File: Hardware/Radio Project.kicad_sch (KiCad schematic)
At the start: 4 parts, among them J1 RJ45_Abracon_ARJP11A-MASA-B-A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, U1 Si4464, U2 Si4464, U3 STM32F407VGT6

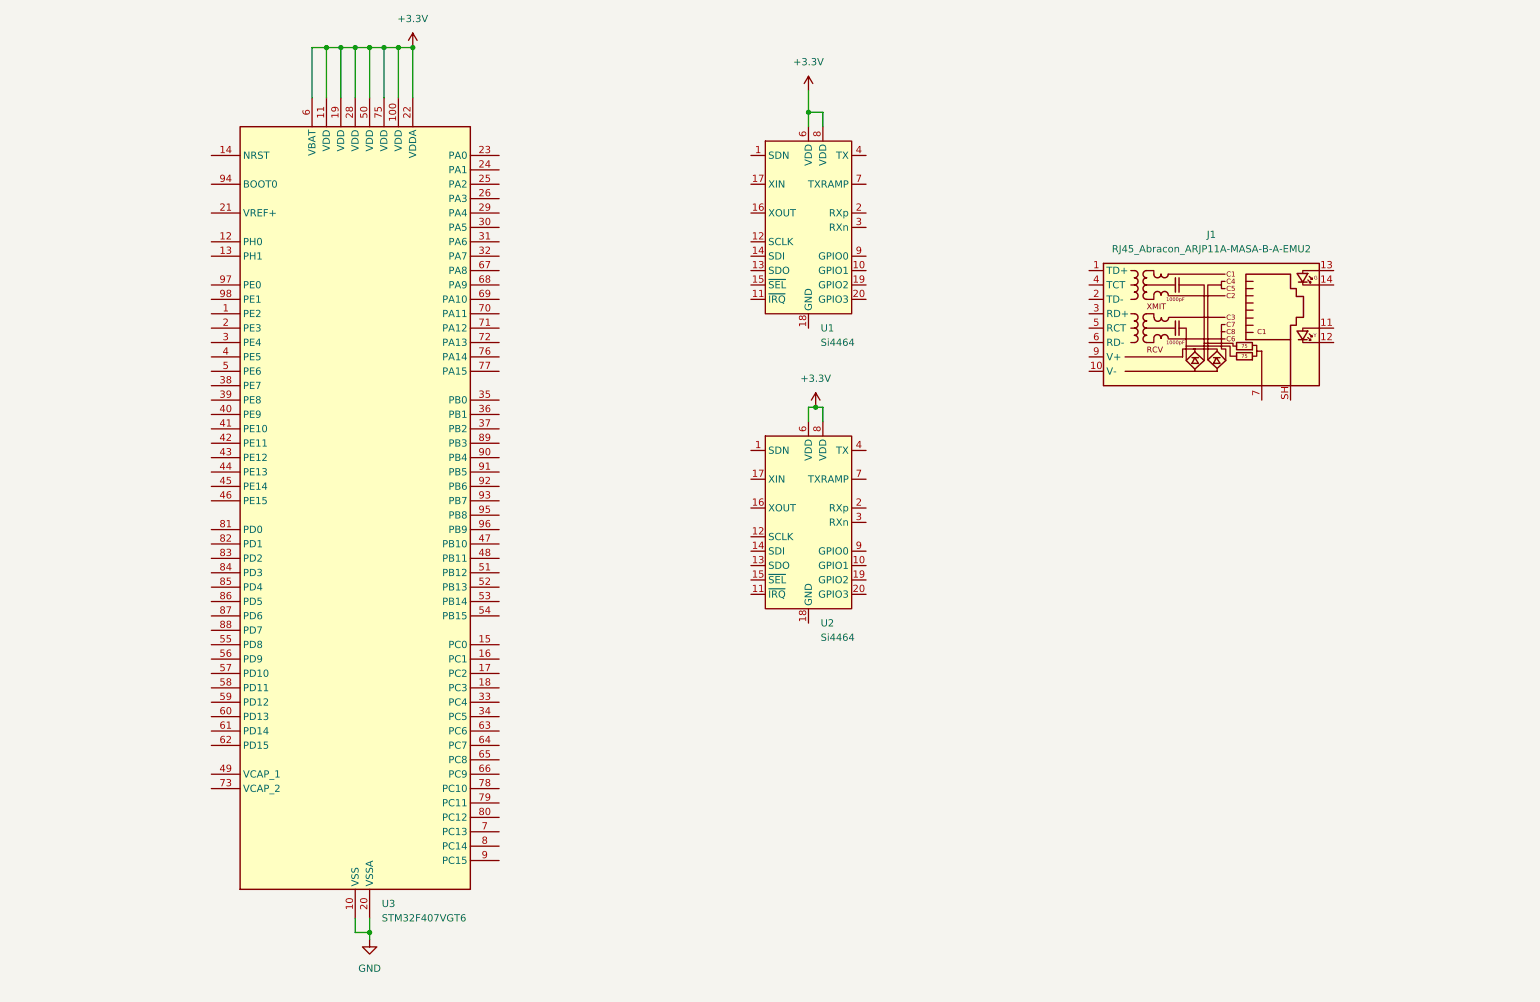
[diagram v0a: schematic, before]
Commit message: added SWD header and dip switches for boot modes
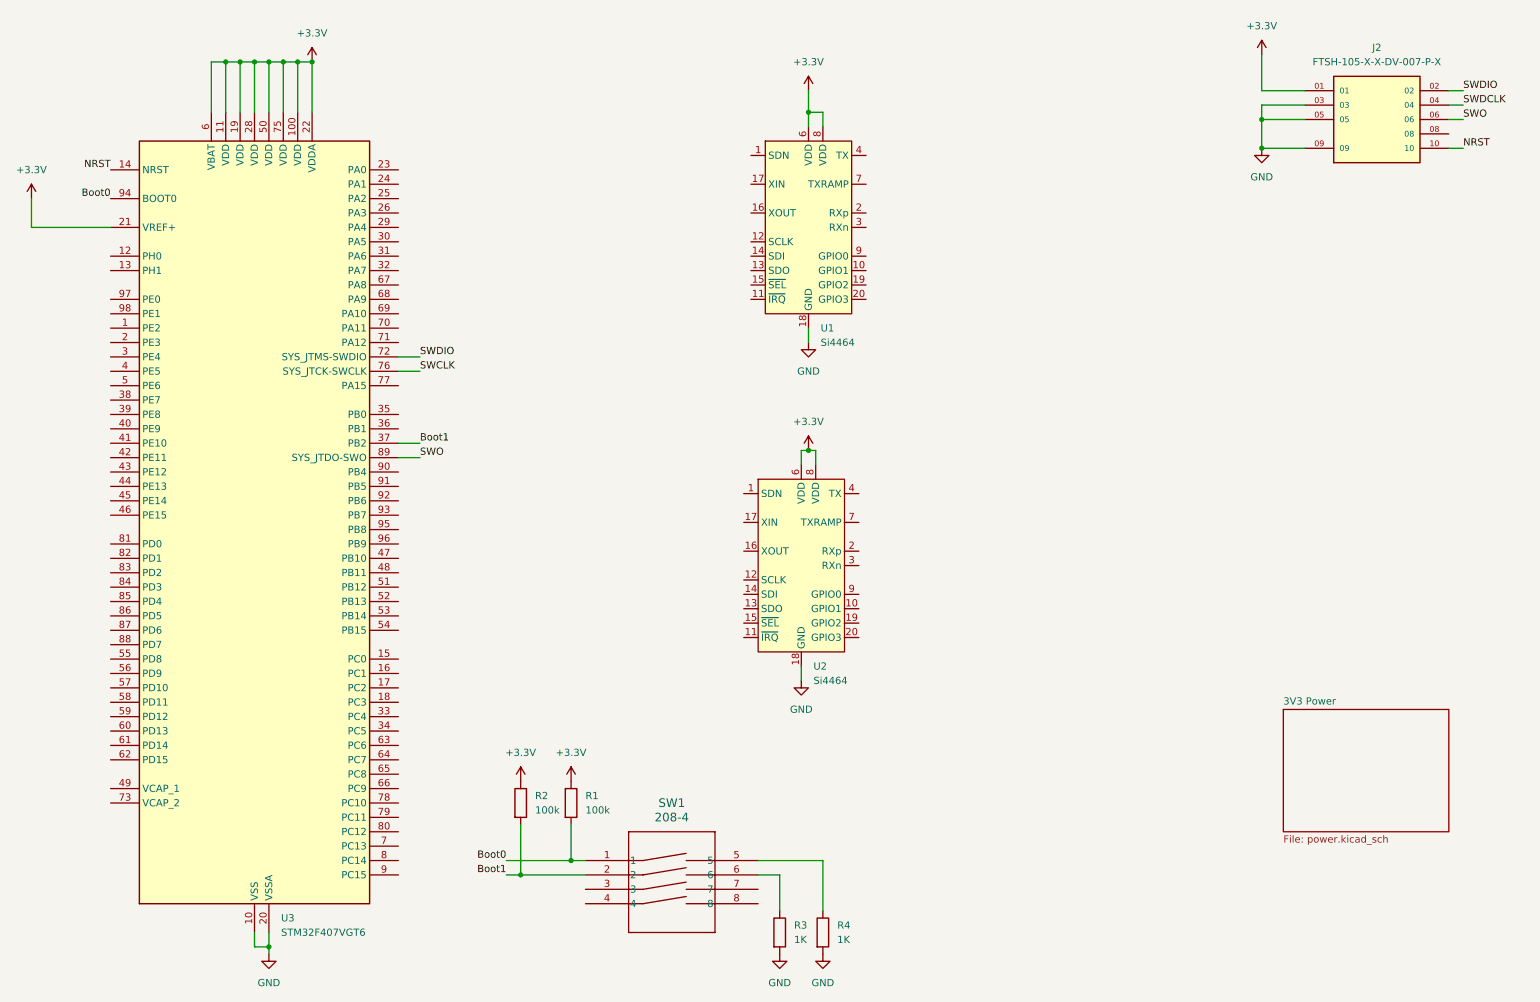
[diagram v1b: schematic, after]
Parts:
- removed J1: RJ45_Abracon_ARJP11A-MASA-B-A-EMU2, Connector_RJ:RJ45_Abracon_ARJP11A-MA_Horizontal, symbol Connector:RJ45_Abracon_ARJP11A-MASA-B-A-EMU2
- added J2: FTSH-105-X-X-DV-007-P-X, FTSH-105-01-L-DV-007-K:SAMTEC_FTSH-105-X-X-DV-007-P-X, symbol SWD Header:FTSH-105-X-X-DV-007-P-X
- added R1, R2: 100k, Resistor_SMD:R_0402_1005Metric, symbol Device:R
- added R3, R4: 1K, Resistor_SMD:R_0402_1005Metric, symbol Device:R
- added SW1: 208-4, 208-4:DIP8_208-4_CTS, symbol 4 POS Dip Switch:208-4
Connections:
- net +3.3V: now also U3.21 (VREF+), J2.01, R1.1, R2.1
- net GND: now also U1.18 (GND), U1.21 (GND), U2.18 (GND), U2.21 (GND), J2.03, J2.05, J2.09, R3.2, R4.2
- net NRST: now reaches U3.14 (NRST)
- net NRST: now also J2.10
- net Boot1: now reaches U3.37 (PB2)
- net Boot1: now also R2.2, SW1.2
- net SWDIO: now reaches U3.72 (PA13)
- net SWDIO: now also J2.02
- net SWCLK: now reaches U3.76 (PA14)
- net SWO: now reaches U3.89 (PB3)
- net SWO: now also J2.06
- net Boot0: now reaches U3.94 (BOOT0)
- net Boot0: now also R1.2, SW1.1
- new net: R4.1, SW1.5
- new net: R3.1, SW1.6
- new net SWDCLK: J2.04
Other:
- added sheet 3V3 Power (power.kicad_sch)
- company: (none) -> Thomas Montano
- title: (none) -> RF Puck
- moved on the sheet: U2, U3

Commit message: Added 3.3V power connections and a USB-C connector for +5V
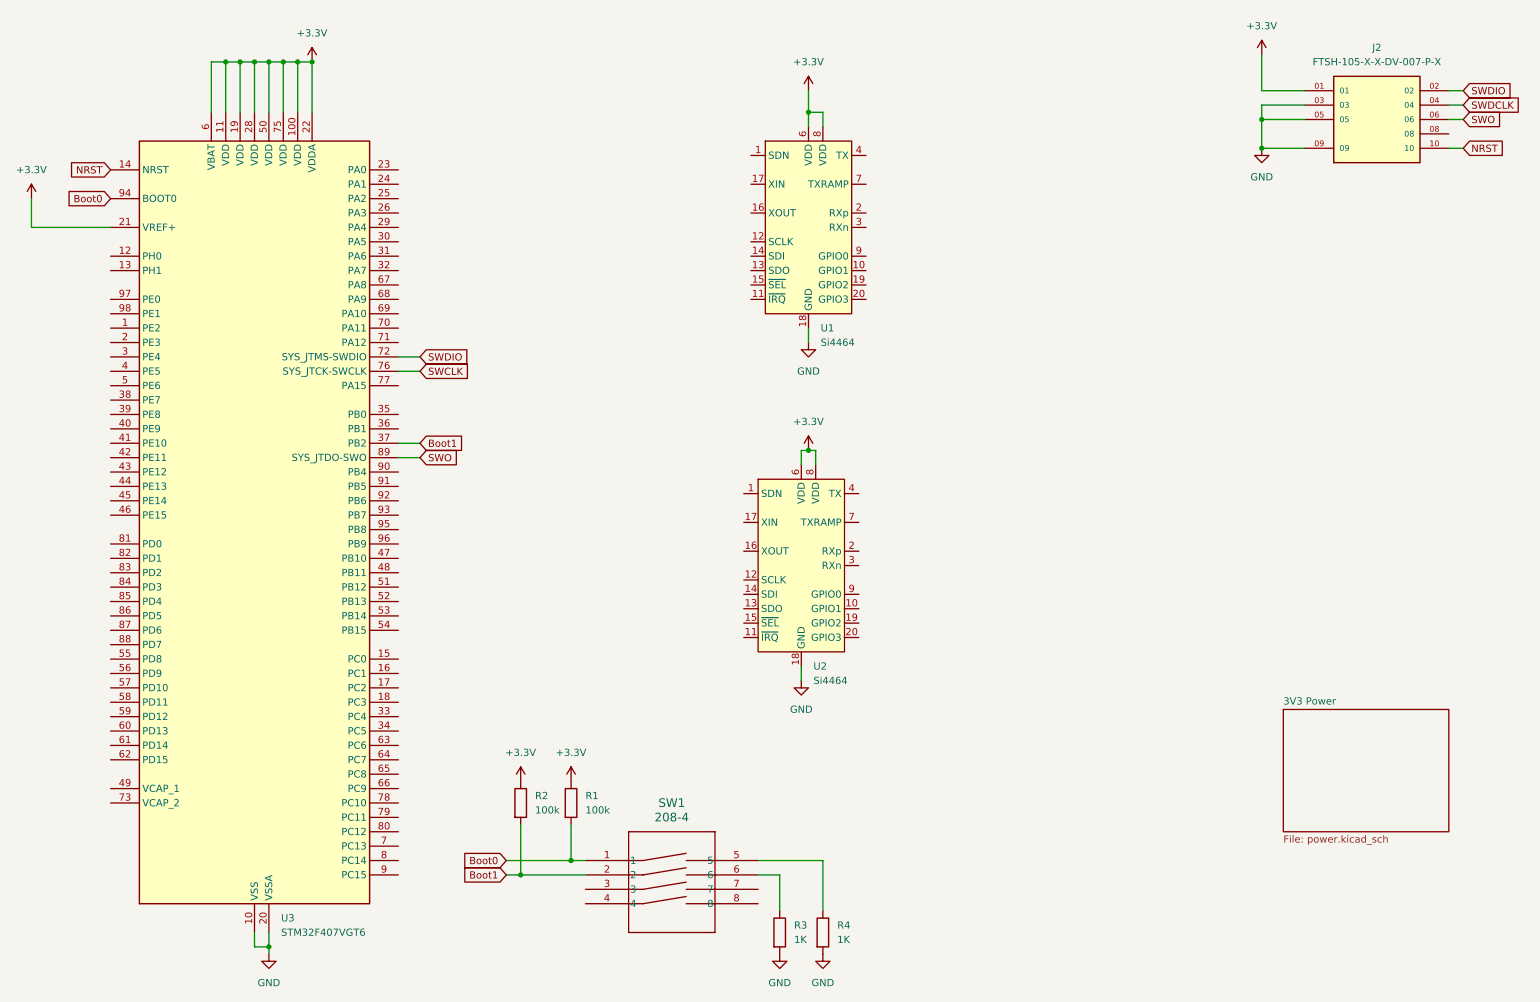
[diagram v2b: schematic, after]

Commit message: added filtering caps, bulk decoupling caps, and power LED
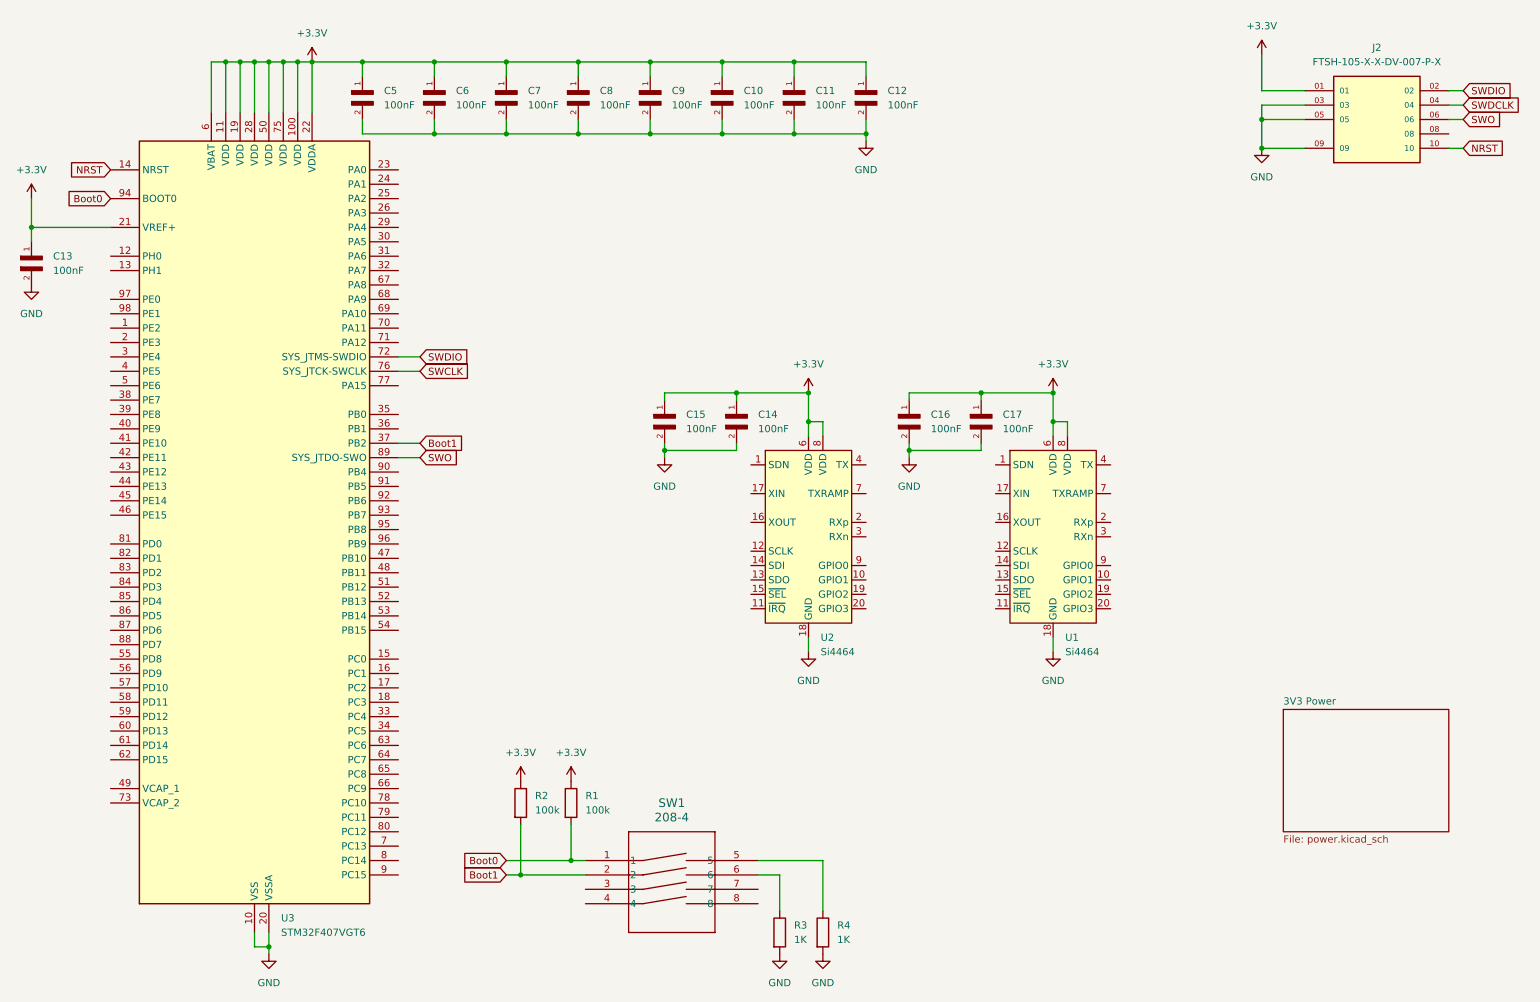
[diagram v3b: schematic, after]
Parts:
- added C10, C11, C12, C13, C14, C15, C16, C17, C5, C6, C7, C8, C9: 100nF, C0402C104J8RACTU:CAPC10555_55N_KEM-L, symbol 2025-06-22_21-59-05:C0402C104J8RACTU
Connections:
- net +3.3V: now also C10.1, C11.1, C12.1, C13.1, C14.1, C15.1, C16.1, C17.1, C5.1, C6.1, C7.1, C8.1, C9.1
- net GND: now also C10.2, C11.2, C12.2, C13.2, C14.2, C15.2, C16.2, C17.2, C5.2, C6.2, C7.2, C8.2, C9.2
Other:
- moved on the sheet: U1, U2

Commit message: added SMA connectors and external connections sheet
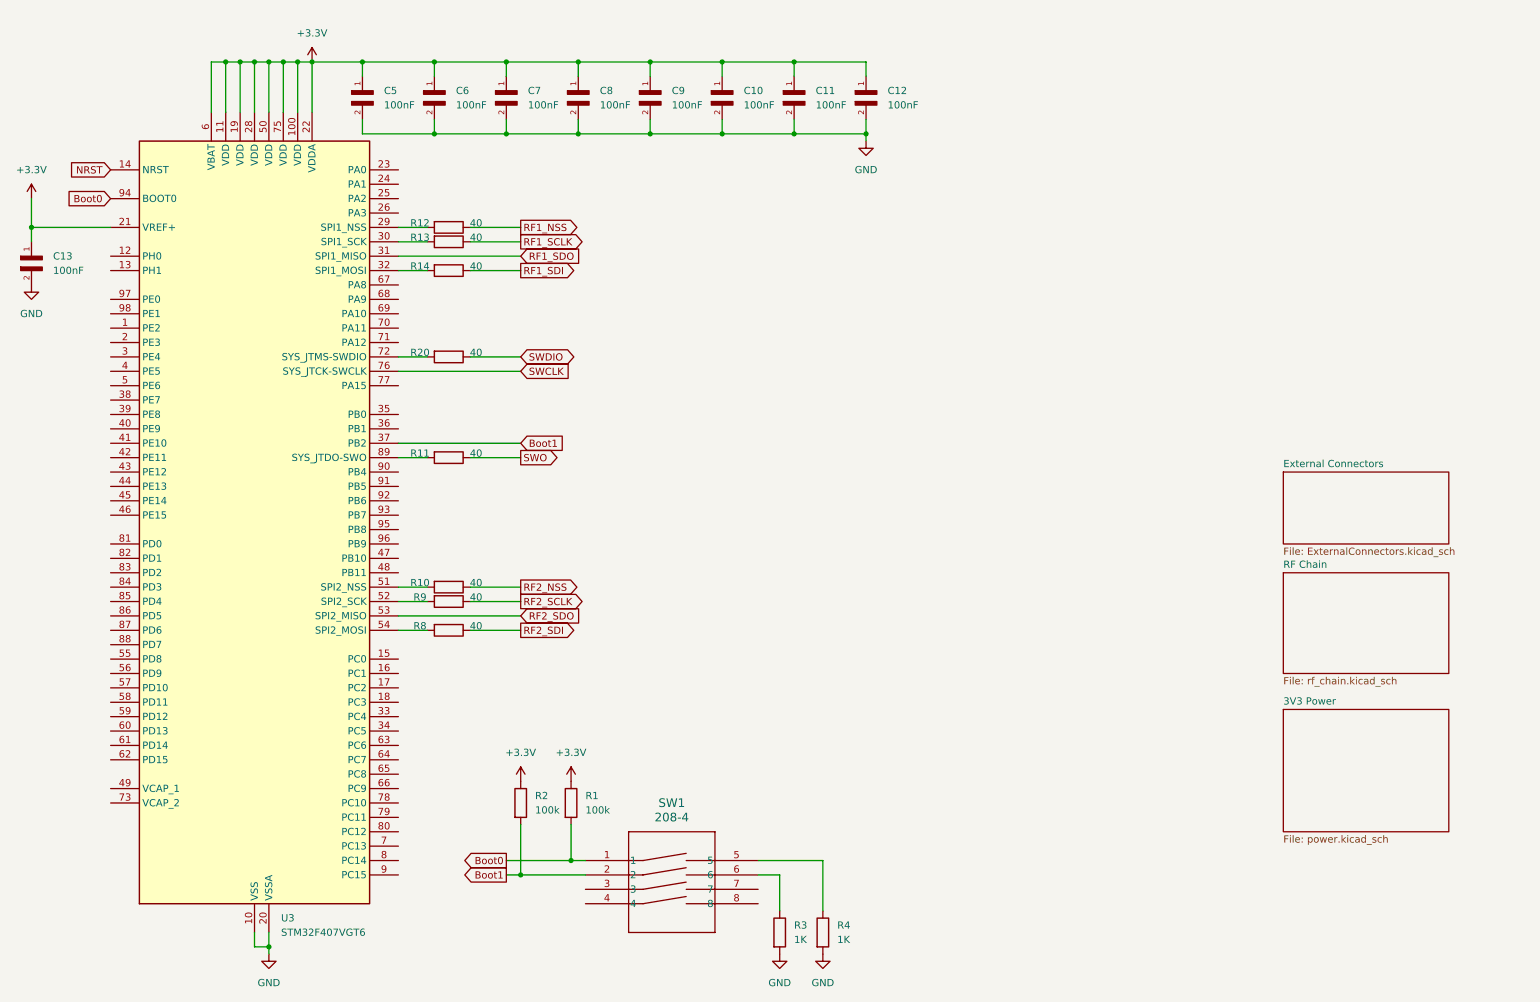
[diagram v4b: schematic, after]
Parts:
- removed C14, C15, C16, C17: 100nF, C0402C104J8RACTU:CAPC10555_55N_KEM-L, symbol 2025-06-22_21-59-05:C0402C104J8RACTU
- removed J2: FTSH-105-X-X-DV-007-P-X, FTSH-105-01-L-DV-007-K:SAMTEC_FTSH-105-X-X-DV-007-P-X, symbol SWD Header:FTSH-105-X-X-DV-007-P-X
- removed U1, U2: Si4464, Package_DFN_QFN:QFN-20-1EP_4x4mm_P0.5mm_EP2.6x2.6mm_ThermalVias, symbol RF:Si4464
- added R10, R11, R12, R13, R14, R20, R8, R9: 40, Resistor_SMD:R_0402_1005Metric, symbol Device:R
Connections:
- net SWDIO: now also R20.1; no longer U3.72 (PA13)
- net SWO: now also R11.1; no longer U3.89 (PB3)
- net at U3.29 (PA4): now also R12.2
- net at U3.30 (PA5): now also R13.2
- net RF1_SDO: now reaches U3.31 (PA6)
- net at U3.32 (PA7): now also R14.2
- net at U3.51 (PB12): now also R10.2
- net at U3.52 (PB13): now also R9.2
- net RF2_SDO: now reaches U3.53 (PB14)
- net at U3.54 (PB15): now also R8.2
- new net: R11.2, U3.89 (PB3)
- new net: R20.2, U3.72 (PA13)
- new net RF1_NSS: R12.1
- new net RF1_SCLK: R13.1
- new net RF1_SDI: R14.1
- new net RF2_NSS: R10.1
- new net RF2_SCLK: R9.1
- new net RF2_SDI: R8.1
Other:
- added sheet External Connectors (ExternalConnectors.kicad_sch)
- added sheet RF Chain (rf_chain.kicad_sch)

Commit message: shutdown pin connection to RF chain
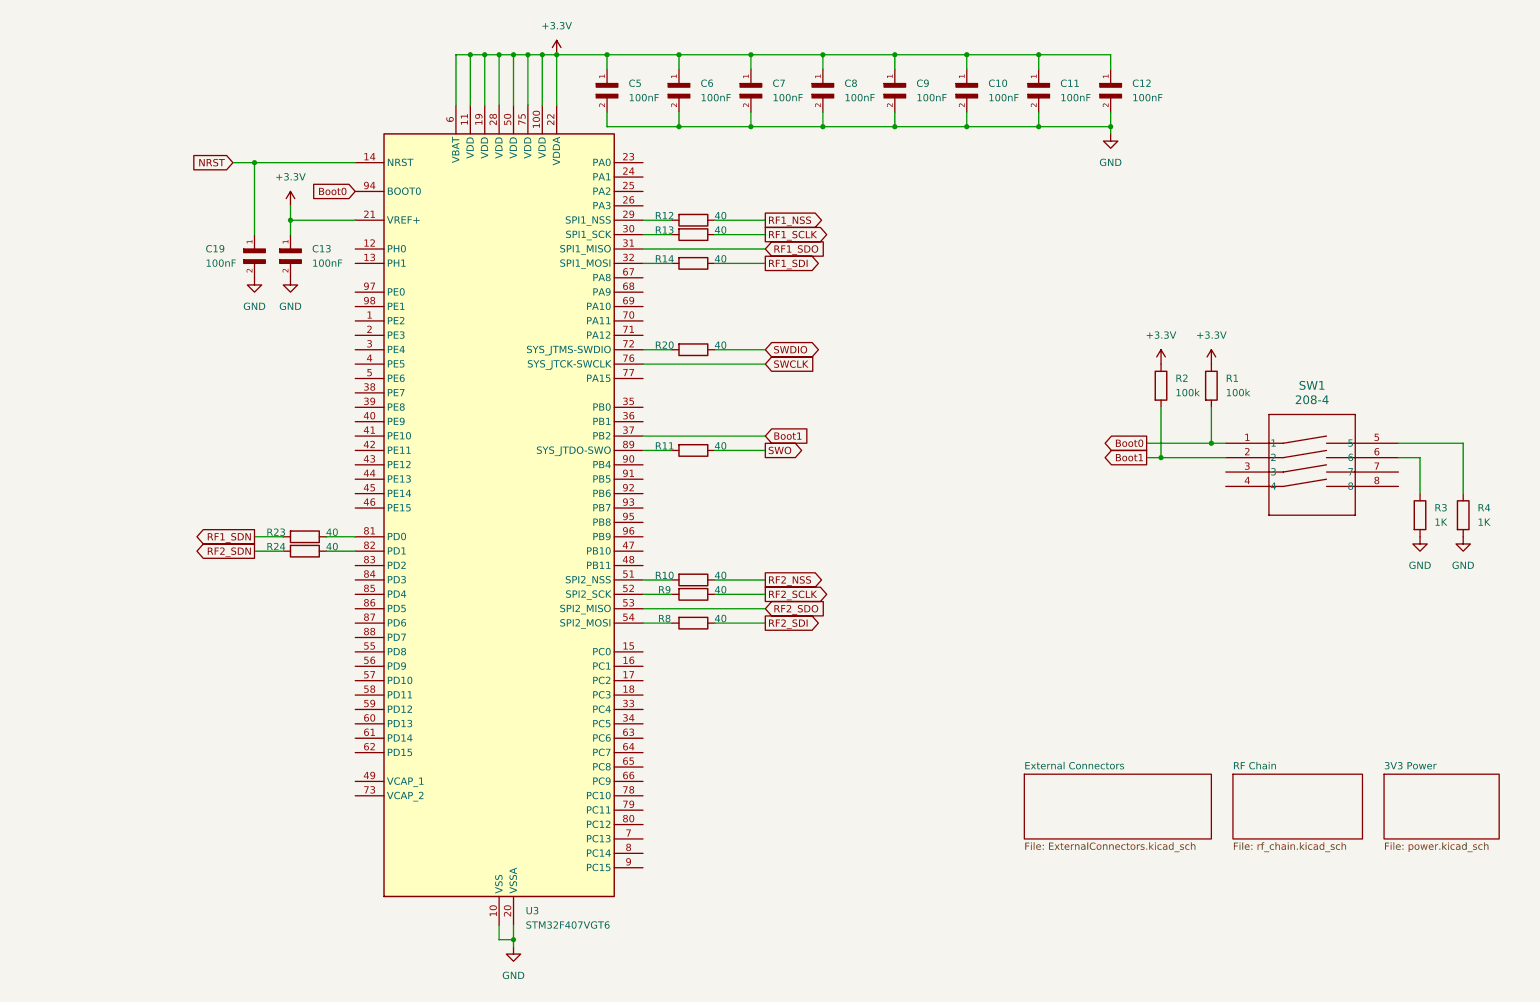
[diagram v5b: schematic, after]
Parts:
- added C19: 100nF, C0402C104J8RACTU:CAPC10555_55N_KEM-L, symbol 2025-06-22_21-59-05:C0402C104J8RACTU
- added R23, R24: 40, Resistor_SMD:R_0402_1005Metric, symbol Device:R
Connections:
- net GND: now also C19.2
- net NRST: now also C19.1
- net at U3.81 (PD0): now also R23.1
- net at U3.82 (PD1): now also R24.1
- new net RF1_SDN: R23.2
- new net RF2_SDN: R24.2
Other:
- moved on the sheet: C10, C11, C12, C13, C5, C6, C7, C8, C9, R1, R10, R11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
